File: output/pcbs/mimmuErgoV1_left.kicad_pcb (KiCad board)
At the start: 2 copper layers, 144.7 x 96.9 mm, 47 parts

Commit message: Add files via upload
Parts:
- moved _3 4.07 mm to (181.6, 153.7), turned to -6 degrees
- moved S3 2.32 mm to (76.7, 170.2), turned to 16 degrees
- moved S6 2.31 mm to (114.0, 142.5), turned to 6 degrees
- moved S9 2.30 mm to (135.7, 134.4), turned to 0 degrees
- moved _2 2.25 mm to (147.5, 134.3), turned to -6 degrees
- moved D3 2.25 mm to (78.1, 175.0), turned to 16 degrees
- moved D6 2.23 mm to (114.5, 147.5), turned to 6 degrees
- moved _1 2.22 mm to (125.8, 142.9), turned to 0 degrees
- moved D9 2.21 mm to (135.7, 139.4), turned to 0 degrees
- moved S2 2.17 mm to (94.0, 165.2), turned to 16 degrees
- moved S12 2.13 mm to (157.8, 139.6), turned to -6 degrees
- moved _9 2.13 mm to (87.4, 175.0), turned to 16 degrees
- moved D2 2.09 mm to (95.4, 170.0), turned to 16 degrees
- moved D12 2.04 mm to (157.2, 144.6), turned to -6 degrees
- moved S5 2.04 mm to (115.7, 159.4), turned to 6 degrees
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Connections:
- D2 pad 1: P9 -> P6
- D3 pad 1: P6 -> P9
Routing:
- net P18: track 0.00 -> 199.4 mm
- net P15: track 0.00 -> 161.8 mm
- net P9: track 0.00 -> 152.3 mm
- net P14: track 0.00 -> 151.8 mm
- net P6: track 0.00 -> 147.5 mm
- net P16: track 0.00 -> 145.4 mm, vias 0 -> 1
- net P8: track 0.00 -> 142.8 mm
- net P10: track 0.00 -> 106.8 mm
- net P7: track 0.00 -> 84.0 mm
- net GND: track 0.00 -> 67.5 mm
- net P2: track 0.00 -> 43.7 mm
- net VCC: track 0.00 -> 43.3 mm
- net P3: track 0.00 -> 42.0 mm
- net P19: track 0.00 -> 35.9 mm
- net P20: track 0.00 -> 34.1 mm
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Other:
- board size 144.7 x 96.9 mm -> 144.3 x 95.7 mm
- net class Default removed

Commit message: finalize
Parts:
- moved TRRS1 64.9 mm to (264.6, 160.7)
- moved D2 64.8 mm to (158.0, 153.5)
- moved S1 64.8 mm to (161.3, 165.1)
- moved S17 64.8 mm to (252.0, 190.0)
- moved S7 64.8 mm to (198.4, 151.9)
- moved _6 64.8 mm to (230.0, 172.1)
- moved S5 64.8 mm to (178.4, 142.9)
- moved _9 64.8 mm to (150.1, 158.6)
- moved D10 64.8 mm to (216.3, 161.9)
- moved S8 64.8 mm to (198.4, 134.9)
- moved D8 64.8 mm to (198.4, 139.9)
- moved D12 64.8 mm to (219.9, 128.1)
- moved S2 64.8 mm to (156.7, 148.7)
- moved _1 64.8 mm to (188.5, 126.4)
- moved S13 64.8 mm to (234.5, 161.8)
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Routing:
- net P14: track 151.8 -> 122.6 mm
- net P18: track 199.4 -> 187.2 mm
- net P15: track 161.8 -> 150.9 mm
- net P16: track 145.4 -> 136.3 mm, vias 1 -> 0
- net P8: track 142.8 -> 138.8 mm
- net GND: track 67.5 -> 64.4 mm
- net P2: track 43.7 -> 41.4 mm
- net P9: track 152.3 -> 150.1 mm
- net middle_top: track 14.9 -> 16.8 mm
- net layer_cluster: track 14.9 -> 16.8 mm
- net middle_bottom: track 14.9 -> 16.8 mm
- net pinkie_top: track 14.9 -> 16.8 mm
- net pinkie_bottom: track 14.9 -> 16.8 mm
- net ring_bottom: track 14.9 -> 16.8 mm
- net space_cluster: track 14.9 -> 16.8 mm
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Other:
- outline, holes or cut-outs redrawn
- board text added: "kubujuss v1"

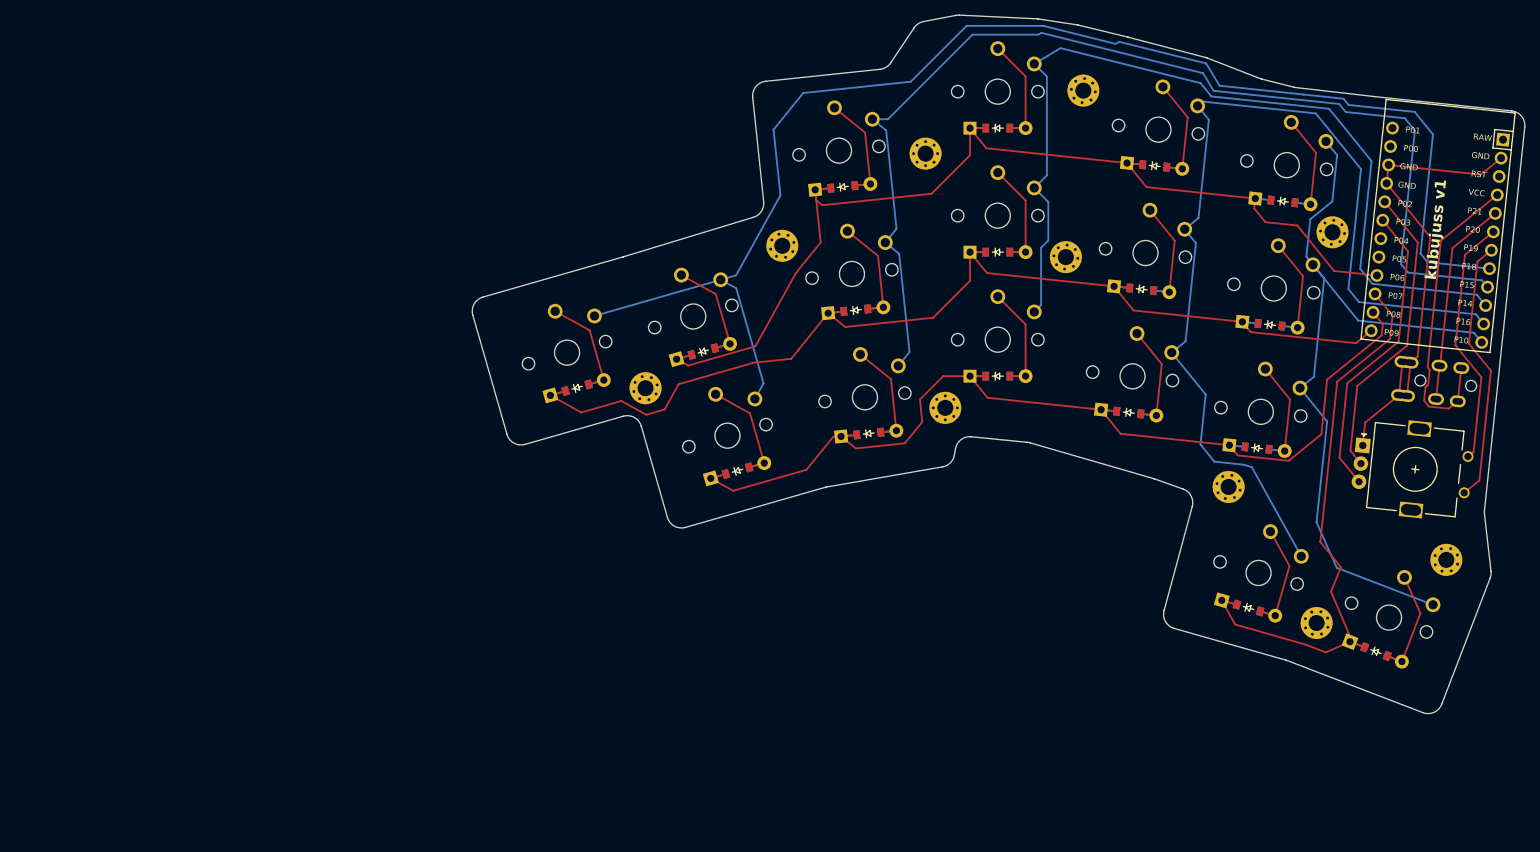
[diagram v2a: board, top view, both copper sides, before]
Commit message: Make GND and VCC traces 1mm thicker
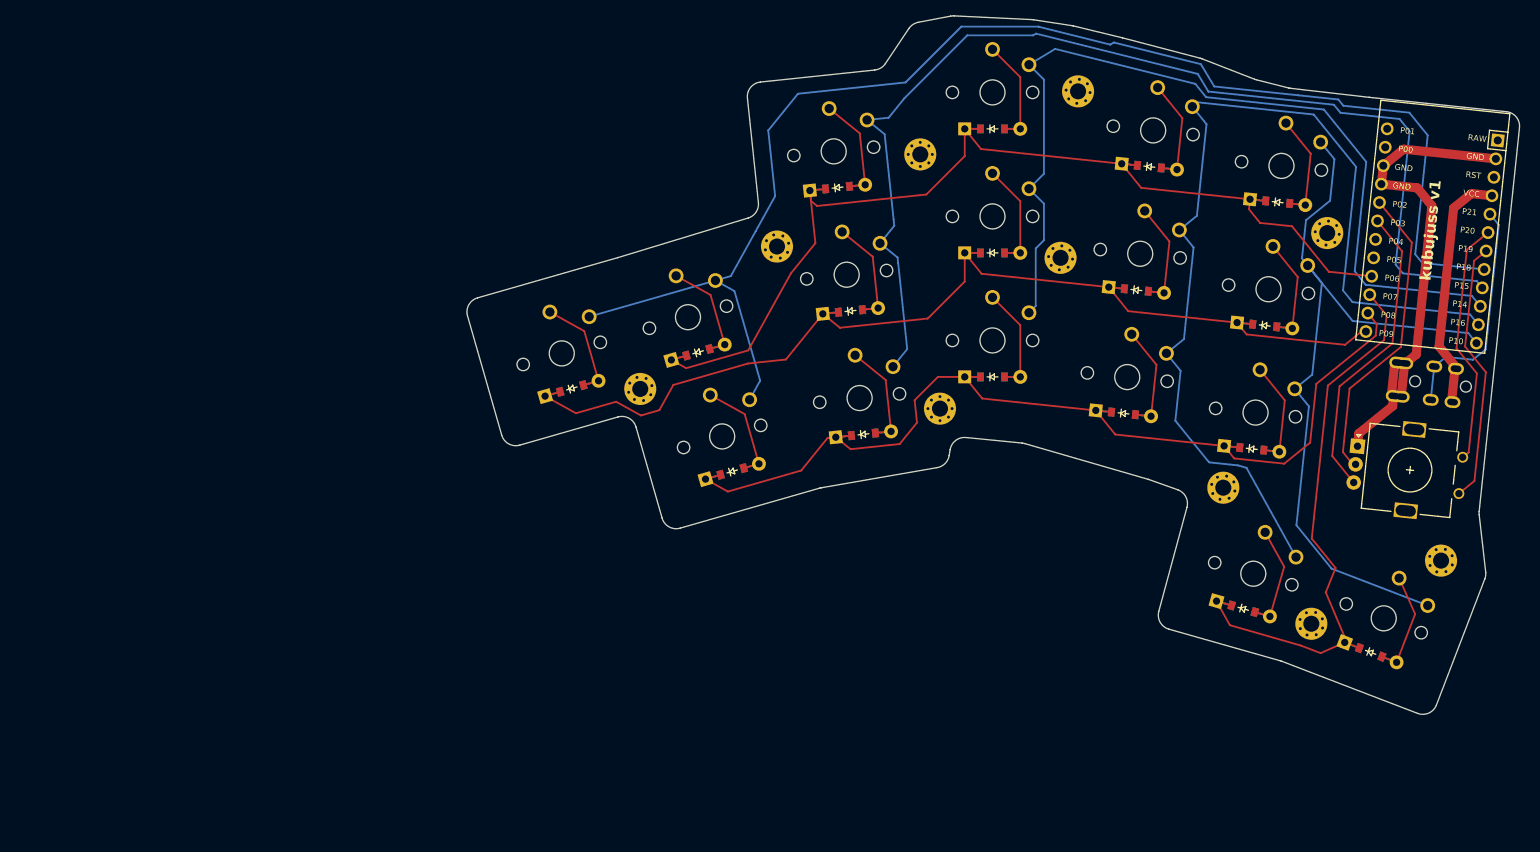
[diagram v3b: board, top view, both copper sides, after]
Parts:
- moved TRRS1 0.73 mm to (263.9, 160.8)
- moved MCU1 0.73 mm to (257.9, 137.7)
- moved _10 0.73 mm to (168.1, 139.1)
- moved _5 0.73 mm to (241.4, 190.8)
- moved _2 0.73 mm to (209.4, 117.9)
- moved D17 0.73 mm to (249.5, 194.8)
- moved S15 0.73 mm to (237.3, 128.1)
- moved D8 0.73 mm to (197.7, 140.0)
- moved D11 0.73 mm to (217.4, 145.1)
- moved D12 0.73 mm to (219.2, 128.2)
- moved S12 0.73 mm to (219.7, 123.2)
- moved _1 0.73 mm to (187.8, 126.5)
- moved D5 0.73 mm to (178.2, 148.0)
- moved D16 0.73 mm to (232.0, 188.8)
- moved S16 0.73 mm to (233.4, 184.0)
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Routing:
- net VCC: track 42.2 -> 33.3 mm
- net GND: track 64.4 -> 68.6 mm
- net P21: track 28.4 -> 31.7 mm
- net P8: track 138.8 -> 141.4 mm
- net P6: track 148.0 -> 150.5 mm
- net P9: track 150.1 -> 152.4 mm
- net inner_bottom: track 14.6 -> 16.8 mm
- net index_home: track 14.6 -> 16.8 mm
- net inner_top: track 14.6 -> 16.8 mm
- net inner_home: track 14.6 -> 16.8 mm
- net P10: track 106.0 -> 107.0 mm
- net P16: track 136.3 -> 137.4 mm
- net P15: track 150.9 -> 151.8 mm
- net P20: track 34.4 -> 33.7 mm
- net P14: track 122.6 -> 123.1 mm
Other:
- outline, holes or cut-outs redrawn
